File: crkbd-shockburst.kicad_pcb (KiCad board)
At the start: 4 copper layers, 0 parts

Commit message: Layout
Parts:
- added Ant101: antenna, RF_Antenna:Texas_SWRA117D_2.4GHz_Right, F.Cu at (131.8, 53.6)
- added Ant102: antenna, RF_Antenna:Texas_SWRA117D_2.4GHz_Right, F.Cu at (155.8, 53.6)
- added Ant601: antenna, RF_Antenna:Texas_SWRA117D_2.4GHz_Right, F.Cu at (31.6, 128.8)
- added BT201: Battery_Cell, connectors:1x2_2.54mm, F.Cu at (128.8, 72.0)
- added BT501: Battery_Cell, connectors:1x2_2.54mm, F.Cu at (169.2, 69.0)
- added C201: 4.7u, passive:C_0603, F.Cu at (134.1, 69.2)
- added C202: 4.7u, passive:C_0603, F.Cu at (131.3, 71.0)
- added C203: 4.7u, passive:C_0603, F.Cu at (145.7, 59.1)
- added C204: 1u, passive:C_0402, F.Cu at (141.6, 63.5)
- added C205: 100n, passive:C_0402, F.Cu at (139.8, 55.0)
- added C206: 4.7u, passive:C_0603, F.Cu at (145.7, 57.9)
- added C207: 4.7u, passive:C_0603, F.Cu at (145.7, 56.7)
- added C208: 4.7u, passive:C_0603, F.Cu at (144.2, 55.2)
- added C209: 1u, passive:C_0402, F.Cu at (144.1, 63.5)
- added C210: 100n, passive:C_0402, F.Cu at (137.9, 63.5)
- added C211: 100n, passive:C_0402, F.Cu at (145.7, 61.1)
- added C212: 100p, passive:C_0402, F.Cu at (136.4, 60.5)
- added C213: 100n, passive:C_0402, F.Cu at (141.3, 64.8)
- added C214: 820p, passive:C_0402, F.Cu at (136.4, 56.6)
- added C215: 16p, passive:C_0402, F.Cu at (136.4, 63.9)
- added C216: 16p, passive:C_0402, F.Cu at (134.9, 62.2)
- added C219: 100n, passive:C_0402, F.Cu at (139.4, 63.1)
- added C220: ~, passive:C_0402, F.Cu at (131.3, 54.5)
- added C221: ~, passive:C_0402, F.Cu at (131.3, 57.2)
- added C222: 1.2p, passive:C_0402, F.Cu at (134.2, 59.1)
- added C223: 1p, passive:C_0402, F.Cu at (136.8, 59.1)
- added C501: 1u, passive:C_0402, F.Cu at (165.6, 63.5)
- added C502: 100n, passive:C_0402, F.Cu at (165.3, 64.8)
- added C503: 4.7u, passive:C_0603, F.Cu at (168.2, 55.2)
- added C504: 100n, passive:C_0402, F.Cu at (169.7, 61.1)
- added C505: 100p, passive:C_0402, F.Cu at (160.4, 60.5)
- added C506: 820p, passive:C_0402, F.Cu at (160.4, 57.5)
- added C507: 100n, passive:C_0402, F.Cu at (163.8, 55.0)
- added C508: 100n, passive:C_0402, F.Cu at (161.9, 63.5)
- added C509: 1u, passive:C_0402, F.Cu at (168.1, 63.5)
- added C510: 4.7u, passive:C_0603, F.Cu at (169.7, 59.1)
- added C511: 4.7u, passive:C_0603, F.Cu at (169.7, 57.9)
- added C512: 4.7u, passive:C_0603, F.Cu at (169.7, 56.7)
- added C513: ~, passive:C_0402, F.Cu at (155.3, 54.5)
- added C514: ~, passive:C_0402, F.Cu at (155.3, 57.2)
- added C515: 1.2p, passive:C_0402, F.Cu at (158.2, 59.1)
- added C516: 1p, passive:C_0402, F.Cu at (160.8, 59.1)
- added C517: 16p, passive:C_0402, F.Cu at (158.9, 62.2)
- added C518: 16p, passive:C_0402, F.Cu at (160.4, 63.9)
- added C519: 100n, passive:C_0402, F.Cu at (163.4, 63.1)
- added C520: 4.7u, passive:C_0603, F.Cu at (162.8, 68.7)
- added C521: 4.7u, passive:C_0603, F.Cu at (166.4, 67.5)
- added C601: 1u, passive:C_0402, F.Cu at (43.7, 120.7)
- added C602: 100n, passive:C_0402, F.Cu at (43.7, 119.8)
- added C603: 4.7u, passive:C_0603, F.Cu at (35.5, 119.0)
- added C604: 100n, passive:C_0402, F.Cu at (41.4, 117.5)
- added C605: 100p, passive:C_0402, F.Cu at (40.6, 126.8)
- added C606: 820p, passive:C_0402, F.Cu at (37.6, 126.8)
- added C607: 100n, passive:C_0402, F.Cu at (35.2, 123.3)
- added C608: 100n, passive:C_0402, F.Cu at (43.8, 125.1)
- added C609: 1u, passive:C_0402, F.Cu at (43.7, 118.8)
- added C610: 4.7u, passive:C_0603, F.Cu at (39.3, 117.6)
- added C611: 4.7u, passive:C_0603, F.Cu at (38.1, 117.6)
- added C612: 4.7u, passive:C_0603, F.Cu at (36.9, 117.6)
- added C613: ~, passive:C_0402, F.Cu at (32.5, 129.2)
- added C614: ~, passive:C_0402, F.Cu at (35.2, 129.2)
- added C615: 1.2p, passive:C_0402, F.Cu at (37.9, 129.2)
- added C616: 1p, passive:C_0402, F.Cu at (39.3, 126.3)
- added C617: 16p, passive:C_0402, F.Cu at (44.2, 127.2)
- added C618: 16p, passive:C_0402, F.Cu at (44.2, 126.2)
- added D201: RED, Diode_SMD:D_0603_1608Metric, F.Cu at (146.2, 54.6)
- added D301: BAT43W, Diode_SMD:D_SOD-123, F.Cu at (31.2, 65.2)
- added D302: BAT43W, Diode_SMD:D_SOD-123, F.Cu at (50.2, 65.2)
- added D303: BAT43W, Diode_SMD:D_SOD-123, F.Cu at (69.2, 60.2)
- added D304: BAT43W, Diode_SMD:D_SOD-123, F.Cu at (88.2, 57.8)
- added D305: BAT43W, Diode_SMD:D_SOD-123, F.Cu at (107.2, 60.2)
- added D306: BAT43W, Diode_SMD:D_SOD-123, F.Cu at (126.2, 62.8)
- added D307: BAT43W, Diode_SMD:D_SOD-123, F.Cu at (31.2, 84.2)
- added D308: BAT43W, Diode_SMD:D_SOD-123, F.Cu at (50.2, 84.2)
- added D309: BAT43W, Diode_SMD:D_SOD-123, F.Cu at (69.2, 79.2)
- added D310: BAT43W, Diode_SMD:D_SOD-123, F.Cu at (88.2, 76.8)
- added D311: BAT43W, Diode_SMD:D_SOD-123, F.Cu at (107.2, 79.2)
- added D312: BAT43W, Diode_SMD:D_SOD-123, F.Cu at (126.2, 81.9)
- added D313: BAT43W, Diode_SMD:D_SOD-123, F.Cu at (31.2, 103.2)
- added D314: BAT43W, Diode_SMD:D_SOD-123, F.Cu at (50.2, 103.2)
- added D315: BAT43W, Diode_SMD:D_SOD-123, F.Cu at (69.2, 98.2)
- added D316: BAT43W, Diode_SMD:D_SOD-123, F.Cu at (88.2, 95.8)
- added D317: BAT43W, Diode_SMD:D_SOD-123, F.Cu at (107.2, 98.2)
- added D318: BAT43W, Diode_SMD:D_SOD-123, F.Cu at (126.2, 100.8)
- added D319: BAT43W, Diode_SMD:D_SOD-123, F.Cu at (97.2, 112.8)
- added D320: BAT43W, Diode_SMD:D_SOD-123, F.Cu at (117.0, 112.0)
- added D321: BAT43W, Diode_SMD:D_SOD-123, F.Cu at (127.8, 112.8)
- added D401: BAT43W, Diode_SMD:D_SOD-123, F.Cu at (266.8, 65.2)
- added D402: BAT43W, Diode_SMD:D_SOD-123, F.Cu at (247.8, 65.2)
- added D403: BAT43W, Diode_SMD:D_SOD-123, F.Cu at (228.8, 60.2)
- added D404: BAT43W, Diode_SMD:D_SOD-123, F.Cu at (209.8, 57.8)
- added D405: BAT43W, Diode_SMD:D_SOD-123, F.Cu at (190.8, 60.2)
- added D406: BAT43W, Diode_SMD:D_SOD-123, F.Cu at (171.8, 62.8)
- added D407: BAT43W, Diode_SMD:D_SOD-123, F.Cu at (266.8, 84.2)
- added D408: BAT43W, Diode_SMD:D_SOD-123, F.Cu at (247.8, 84.2)
- added D409: BAT43W, Diode_SMD:D_SOD-123, F.Cu at (228.8, 79.2)
- added D410: BAT43W, Diode_SMD:D_SOD-123, F.Cu at (209.8, 76.8)
- added D411: BAT43W, Diode_SMD:D_SOD-123, F.Cu at (190.8, 79.2)
- added D412: BAT43W, Diode_SMD:D_SOD-123, F.Cu at (171.8, 81.9)
- added D413: BAT43W, Diode_SMD:D_SOD-123, F.Cu at (266.8, 103.2)
- added D414: BAT43W, Diode_SMD:D_SOD-123, F.Cu at (247.8, 103.2)
- added D415: BAT43W, Diode_SMD:D_SOD-123, F.Cu at (228.8, 98.2)
- added D416: BAT43W, Diode_SMD:D_SOD-123, F.Cu at (209.8, 95.8)
- added D417: BAT43W, Diode_SMD:D_SOD-123, F.Cu at (190.8, 98.2)
- added D418: BAT43W, Diode_SMD:D_SOD-123, F.Cu at (171.8, 100.8)
- added D419: BAT43W, Diode_SMD:D_SOD-123, F.Cu at (200.8, 112.8)
- added D420: BAT43W, Diode_SMD:D_SOD-123, F.Cu at (181.0, 112.0)
- added D421: BAT43W, Diode_SMD:D_SOD-123, F.Cu at (170.2, 112.8)
- added D501: RED, Diode_SMD:D_0603_1608Metric, F.Cu at (151.8, 54.6)
- added D601: RED, Diode_SMD:D_0603_1608Metric, F.Cu at (34.7, 117.1)
- added FB201: FerriteBead_Small, passive:R_0603, F.Cu at (134.1, 71.6)
- added FB501: FerriteBead_Small, passive:R_0603, F.Cu at (161.5, 68.7)
- added FB601: FerriteBead_Small, passive:R_0603, F.Cu at (45.9, 120.5)
- added H201: MountingHole, MountingHole:MountingHole_4.3mm_M4, F.Cu at (31.8, 93.8)
- added H202: MountingHole, MountingHole:MountingHole_4.3mm_M4, F.Cu at (31.8, 74.8)
- added H203: MountingHole, MountingHole:MountingHole_4.3mm_M4, F.Cu at (74.9, 111.0)
- added H204: MountingHole, MountingHole:MountingHole_4.3mm_M4, F.Cu at (107.7, 71.2)
- added H205: MountingHole, MountingHole:MountingHole_4.3mm_M4, F.Cu at (121.5, 118.6)
- added H501: MountingHole, MountingHole:MountingHole_4.3mm_M4, F.Cu at (266.2, 93.8)
- added H502: MountingHole, MountingHole:MountingHole_4.3mm_M4, F.Cu at (266.2, 74.8)
- added H503: MountingHole, MountingHole:MountingHole_4.3mm_M4, F.Cu at (223.1, 111.0)
- added H504: MountingHole, MountingHole:MountingHole_4.3mm_M4, F.Cu at (190.3, 71.2)
- added H505: MountingHole, MountingHole:MountingHole_4.3mm_M4, F.Cu at (176.5, 118.6)
- added J201: USB_C_Receptacle_USB2.0, connectors:USB_C_Receptacle_USB4105, F.Cu at (144.2, 71.8)
- added J202: tag-connect-swd, Connector:Tag-Connect_TC2030-IDC-NL_2x03_P1.27mm_Vertical, F.Cu at (131.2, 63.2)
- added J5: Breakaway_Tabs, kbd:Breakaway_Tabs, F.Cu at (31.7, 55.8)
- added J5: Breakaway_Tabs, kbd:Breakaway_Tabs, F.Cu at (266.3, 55.8)
- added J5: Breakaway_Tabs, kbd:Breakaway_Tabs, F.Cu at (199.2, 130.0)
- added J5: Breakaway_Tabs, kbd:Breakaway_Tabs, F.Cu at (45.8, 132.2)
- added J5: Breakaway_Tabs, kbd:Breakaway_Tabs, F.Cu at (45.8, 116.2)
- added J5: Breakaway_Tabs, kbd:Breakaway_Tabs, F.Cu at (252.3, 112.7)
- added J5: Breakaway_Tabs, kbd:Breakaway_Tabs, F.Cu at (160.2, 47.8)
- added J5: Breakaway_Tabs, kbd:Breakaway_Tabs, F.Cu at (136.2, 47.8)
- added J5: Breakaway_Tabs, kbd:Breakaway_Tabs, F.Cu at (45.8, 112.7)
- added J5: Breakaway_Tabs, kbd:Breakaway_Tabs, F.Cu at (25.8, 124.3)
- added J5: Breakaway_Tabs, kbd:Breakaway_Tabs, F.Cu at (99.1, 130.1)
- added J501: tag-connect-swd, Connector:Tag-Connect_TC2030-IDC-NL_2x03_P1.27mm_Vertical, F.Cu at (155.2, 62.8)
- added J502: USB_C_Receptacle_USB2.0, connectors:USB_C_Receptacle_USB4105, F.Cu at (153.8, 71.8)
- added J601: tag-connect-swd, Connector:Tag-Connect_TC2030-IDC-NL_2x03_P1.27mm_Vertical, B.Cu at (34.7, 124.0)
- added J602: USB_A, usb:USB_A_1001-011-01101, F.Cu at (49.5, 124.2)
- added L201: 10u, passive:R_0603, F.Cu at (143.0, 63.9)
- added L202: 47n, passive:R_0402, F.Cu at (142.7, 65.5)
- added L203: ~, passive:R_0402, F.Cu at (131.8, 55.9)
- added L204: 4.7n, passive:R_0402, F.Cu at (135.5, 58.6)
- added L205: 2.2n, passive:R_0402, F.Cu at (132.8, 58.6)
- added L501: 47n, passive:R_0402, F.Cu at (166.7, 65.5)
- added L502: 10u, passive:R_0603, F.Cu at (167.0, 63.9)
- added L503: ~, passive:R_0402, F.Cu at (155.8, 55.9)
- added L504: 2.2n, passive:R_0402, F.Cu at (156.8, 58.6)
- added L505: 4.7n, passive:R_0402, F.Cu at (159.5, 58.6)
- added L603: ~, passive:R_0402, F.Cu at (33.8, 128.8)
- added L604: 2.2n, passive:R_0402, F.Cu at (36.5, 128.8)
- added L605: 4.7n, passive:R_0402, F.Cu at (38.9, 127.7)
- added R101: 1k, passive:R_0402, F.Cu at (136.4, 57.6)
- added R201: 1M, passive:R_0402, F.Cu at (139.4, 65.0)
- added R202: 1M, passive:R_0402, F.Cu at (139.4, 64.0)
- added R203: 5.1k, passive:R_0402, F.Cu at (145.1, 65.3)
- added R204: 5.1k, passive:R_0402, F.Cu at (144.1, 65.3)
- added R205: 1k, passive:R_0402, F.Cu at (145.7, 60.2)
- added R206: 5.1k, passive:R_0402, F.Cu at (134.3, 67.5)
- added R501: 1k, passive:R_0402, F.Cu at (169.7, 60.2)
- added R502: 1M, passive:R_0402, F.Cu at (163.4, 65.0)
- added R503: 1M, passive:R_0402, F.Cu at (163.4, 64.0)
- added R504: 5.1k, passive:R_0402, F.Cu at (158.2, 64.9)
- added R505: 5.1k, passive:R_0402, F.Cu at (158.2, 65.9)
- added R506: 5.1k, passive:R_0402, F.Cu at (164.3, 72.1)
- added R601: 1k, passive:R_0402, F.Cu at (40.4, 117.5)
- added SW301: SW_Push, connectors:Kailh MX hotswap socket, B.Cu at (22.2, 65.2)
- added SW302: SW_Push, connectors:Kailh MX hotswap socket, B.Cu at (41.2, 65.2)
- added SW303: SW_Push, connectors:Kailh MX hotswap socket, B.Cu at (60.2, 60.2)
- added SW304: SW_Push, connectors:Kailh MX hotswap socket, B.Cu at (79.2, 57.8)
- added SW305: SW_Push, connectors:Kailh MX hotswap socket, B.Cu at (98.2, 60.2)
- added SW306: SW_Push, connectors:Kailh MX hotswap socket, B.Cu at (117.2, 62.8)
- added SW307: SW_Push, connectors:Kailh MX hotswap socket, B.Cu at (22.2, 84.2)
- added SW308: SW_Push, connectors:Kailh MX hotswap socket, B.Cu at (41.2, 84.2)
- added SW309: SW_Push, connectors:Kailh MX hotswap socket, B.Cu at (60.2, 79.2)
- added SW310: SW_Push, connectors:Kailh MX hotswap socket, B.Cu at (79.2, 76.8)
- added SW311: SW_Push, connectors:Kailh MX hotswap socket, B.Cu at (98.2, 79.2)
- added SW312: SW_Push, connectors:Kailh MX hotswap socket, B.Cu at (117.2, 81.8)
- added SW313: SW_Push, connectors:Kailh MX hotswap socket, B.Cu at (22.2, 103.2)
- added SW314: SW_Push, connectors:Kailh MX hotswap socket, B.Cu at (41.2, 103.2)
- added SW315: SW_Push, connectors:Kailh MX hotswap socket, B.Cu at (60.2, 98.2)
- added SW316: SW_Push, connectors:Kailh MX hotswap socket, B.Cu at (79.2, 95.8)
- added SW317: SW_Push, connectors:Kailh MX hotswap socket, B.Cu at (98.2, 98.2)
- added SW318: SW_Push, connectors:Kailh MX hotswap socket, B.Cu at (117.2, 100.8)
- added SW319: SW_Push, connectors:Kailh MX hotswap socket, B.Cu at (88.2, 118.2)
- added SW320: SW_Push, connectors:Kailh MX hotswap socket, B.Cu at (109.8, 120.8)
- added SW321: SW_Push, connectors:Kailh MX hotswap socket 1.5u, B.Cu at (132.1, 124.5)
- added SW401: SW_Push, connectors:Kailh MX hotswap socket, B.Cu at (275.8, 65.2)
- added SW402: SW_Push, connectors:Kailh MX hotswap socket, B.Cu at (256.8, 65.2)
- added SW403: SW_Push, connectors:Kailh MX hotswap socket, B.Cu at (237.8, 60.2)
- added SW404: SW_Push, connectors:Kailh MX hotswap socket, B.Cu at (218.8, 57.8)
- added SW405: SW_Push, connectors:Kailh MX hotswap socket, B.Cu at (199.8, 60.2)
- added SW406: SW_Push, connectors:Kailh MX hotswap socket, B.Cu at (180.8, 62.8)
- added SW407: SW_Push, connectors:Kailh MX hotswap socket, B.Cu at (275.8, 84.2)
- added SW408: SW_Push, connectors:Kailh MX hotswap socket, B.Cu at (256.8, 84.2)
- added SW409: SW_Push, connectors:Kailh MX hotswap socket, B.Cu at (237.8, 79.2)
- added SW410: SW_Push, connectors:Kailh MX hotswap socket, B.Cu at (218.8, 76.8)
- added SW411: SW_Push, connectors:Kailh MX hotswap socket, B.Cu at (199.8, 79.2)
- added SW412: SW_Push, connectors:Kailh MX hotswap socket, B.Cu at (180.8, 81.8)
- added SW413: SW_Push, connectors:Kailh MX hotswap socket, B.Cu at (275.8, 103.2)
- added SW414: SW_Push, connectors:Kailh MX hotswap socket, B.Cu at (256.8, 103.2)
- added SW415: SW_Push, connectors:Kailh MX hotswap socket, B.Cu at (237.8, 98.2)
- added SW416: SW_Push, connectors:Kailh MX hotswap socket, B.Cu at (218.8, 95.8)
- added SW417: SW_Push, connectors:Kailh MX hotswap socket, B.Cu at (199.8, 98.2)
- added SW418: SW_Push, connectors:Kailh MX hotswap socket, B.Cu at (180.8, 100.8)
- added SW419: SW_Push, connectors:Kailh MX hotswap socket, B.Cu at (209.8, 118.2)
- added SW420: SW_Push, connectors:Kailh MX hotswap socket, B.Cu at (188.2, 120.8)
- added SW421: SW_Push, connectors:Kailh MX hotswap socket 1.5u, B.Cu at (165.9, 124.5)
- added SW601: SW_Push, Button_Switch_SMD:SW_SPST_EVQP2, F.Cu at (43.5, 129.9)
- added U201: nRF52833-QDxx, Package_DFN_QFN:QFN-40-1EP_5x5mm_P0.4mm_EP3.6x3.6mm, F.Cu at (141.0, 59.2)
- added U202: USBLC6-2SC6, Package_TO_SOT_SMD:SOT-23-6, F.Cu at (136.8, 71.8)
- added U204: MCP73832-2-OT, Package_TO_SOT_SMD:SOT-23-5, F.Cu at (131.3, 68.6)
- added U501: nRF52833-QDxx, Package_DFN_QFN:QFN-40-1EP_5x5mm_P0.4mm_EP3.6x3.6mm, F.Cu at (165.0, 59.2)
- added U502: USBLC6-2SC6, Package_TO_SOT_SMD:SOT-23-6, F.Cu at (161.2, 71.8)
- added U503: MCP73832-2-OT, Package_TO_SOT_SMD:SOT-23-5, F.Cu at (165.5, 69.8)
- added U601: nRF52833-QDxx, Package_DFN_QFN:QFN-40-1EP_5x5mm_P0.4mm_EP3.6x3.6mm, F.Cu at (39.5, 122.2)
- added U602: USBLC6-2SC6, Package_TO_SOT_SMD:SOT-23-6, F.Cu at (45.1, 123.0)
- added Y201: 32 MHz, crystals:Crystal_4Pin_2.0x1.6mm, F.Cu at (136.4, 62.1)
- added Y501: 32 MHz, crystals:Crystal_4Pin_2.0x1.6mm, F.Cu at (160.4, 62.1)
- added Y601: 32 MHz, crystals:Crystal_4Pin_2.0x1.6mm, F.Cu at (42.4, 126.7)
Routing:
- net /Right Keyboard Controller/KIO0: track 0.00 -> 256.9 mm, vias 0 -> 1
- net /Left Keyboard Controller/KIO4: track 0.00 -> 253.3 mm, vias 0 -> 1
- net /Right Keyboard Controller/KIO1: track 0.00 -> 240.0 mm, vias 0 -> 1
- net /Left Keyboard Controller/KIO5: track 0.00 -> 232.5 mm, vias 0 -> 1
- net /Right Keyboard Controller/KIO2: track 0.00 -> 220.2 mm, vias 0 -> 1
- net /Left Keyboard Controller/KIO6: track 0.00 -> 212.6 mm, vias 0 -> 1
- net /Left Keyboard Controller/KIO7: track 0.00 -> 201.3 mm, vias 0 -> 1
- net /Right Keyboard Controller/KIO3: track 0.00 -> 201.0 mm, vias 0 -> 1
- net /Right Keyboard Controller/KIO9: track 0.00 -> 178.8 mm, vias 0 -> 1
- net /Left Keyboard Controller/KIO8: track 0.00 -> 178.0 mm, vias 0 -> 1
- net /Left Keyboard Controller/KIO2: track 0.00 -> 157.8 mm, vias 0 -> 2
- net /Left Keyboard Controller/KIO9: track 0.00 -> 157.7 mm, vias 0 -> 1
- net /Right Keyboard Controller/KIO8: track 0.00 -> 157.4 mm, vias 0 -> 1
- net /Right Keyboard Controller/KIO6: track 0.00 -> 149.6 mm, vias 0 -> 2
- net /Left Keyboard Controller/KIO1: track 0.00 -> 140.5 mm, vias 0 -> 2
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- added copper zone on B.Cu, net GND
- added copper zone on F.Cu, net GND
- added copper zone on In1.Cu, net GND
- added copper zone on In2.Cu, net GND
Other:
- board outline added: 272 x 112 mm
- board text added: "+"
- board text added: "-"
- board text added: "502030 Li-Ion"
- board text added: "BAT"
- board text added: "BATTERY"
- board text added: "By Emil Fresk - @korken89"
- board text added: "Chg = 200 mA"
- board text added: "Corne ShockBurst"
- board text added: "Dongle"
- board text added: "Emil Fresk @korken89"
- board text added: "Rev 1.0"
- board text added: "TM"

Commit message: Save
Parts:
- added REF**: Hirose_FH12-10S-0.5SH_1x10-1MP_P0.50mm_Horizontal, Connector_FFC-FPC:Hirose_FH12-10S-0.5SH_1x10-1MP_P0.50mm_Horizontal, B.Cu at (137.0, 60.0)
- SW301, SW302, SW303, SW304, SW305, SW306, SW307, SW308, SW309, SW310, SW311, SW312, SW313, SW314, SW315, SW316, SW317, SW318, SW319, SW320, SW321, SW401, SW402, SW403, SW404, SW405, SW406, SW407, SW408, SW409, SW410, SW411, SW412, SW413, SW414, SW415, SW416, SW417, SW418, SW419, SW420, SW421: moved to F.Cu
- moved D419 18.5 mm to (217.5, 120.5)
- moved D319 17.6 mm to (80.5, 118.0)
- moved D421 17.6 mm to (175.5, 129.5)
- moved D420 17.5 mm to (196.0, 121.0)
- moved D320 16.8 mm to (102.0, 119.5)
- moved D301 16.8 mm to (14.5, 65.2)
- moved D302 16.8 mm to (33.5, 65.2)
- moved D303 16.8 mm to (52.5, 60.2)
- moved D304 16.8 mm to (71.5, 57.8)
- moved D305 16.8 mm to (90.5, 60.2)
- moved D306 16.8 mm to (109.5, 62.8)
- moved D307 16.8 mm to (14.5, 84.2)
- moved D308 16.8 mm to (33.5, 84.2)
- moved D309 16.8 mm to (52.5, 79.2)
- moved D310 16.8 mm to (71.5, 76.8)
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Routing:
- net /Right Keyboard Controller/KIO0: track 256.9 -> 84.1 mm
- net /Right Keyboard Controller/KIO1: track 240.0 -> 86.3 mm
- net /Right Keyboard Controller/KIO2: track 220.2 -> 84.4 mm
- net /Right Keyboard Controller/KIO3: track 201.0 -> 75.8 mm
- net /Right Keyboard Controller/KIO6: track 149.6 -> 43.7 mm
- net /Right Keyboard Controller/KIO5: track 132.3 -> 27.5 mm
- net /Right Keyboard Controller/KIO4: track 112.0 -> 7.41 mm
- net /Right Keyboard Controller/KIO9: track 178.8 -> 74.3 mm
- net /Right Keyboard Controller/KIO8: track 157.4 -> 73.0 mm
- net /Left Keyboard Controller/KIO9: track 157.7 -> 105.4 mm, vias 1 -> 5
- net /Right Keyboard Controller/KIO7: track 90.3 -> 44.9 mm
- net /Left Keyboard Controller/KIO3: track 90.3 -> 119.7 mm
- net /Left Keyboard Controller/KIO1: track 140.5 -> 159.2 mm
- net /Left Keyboard Controller/KIO0: track 120.0 -> 138.2 mm
- net /Left Keyboard Controller/KIO2: track 157.8 -> 175.7 mm
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
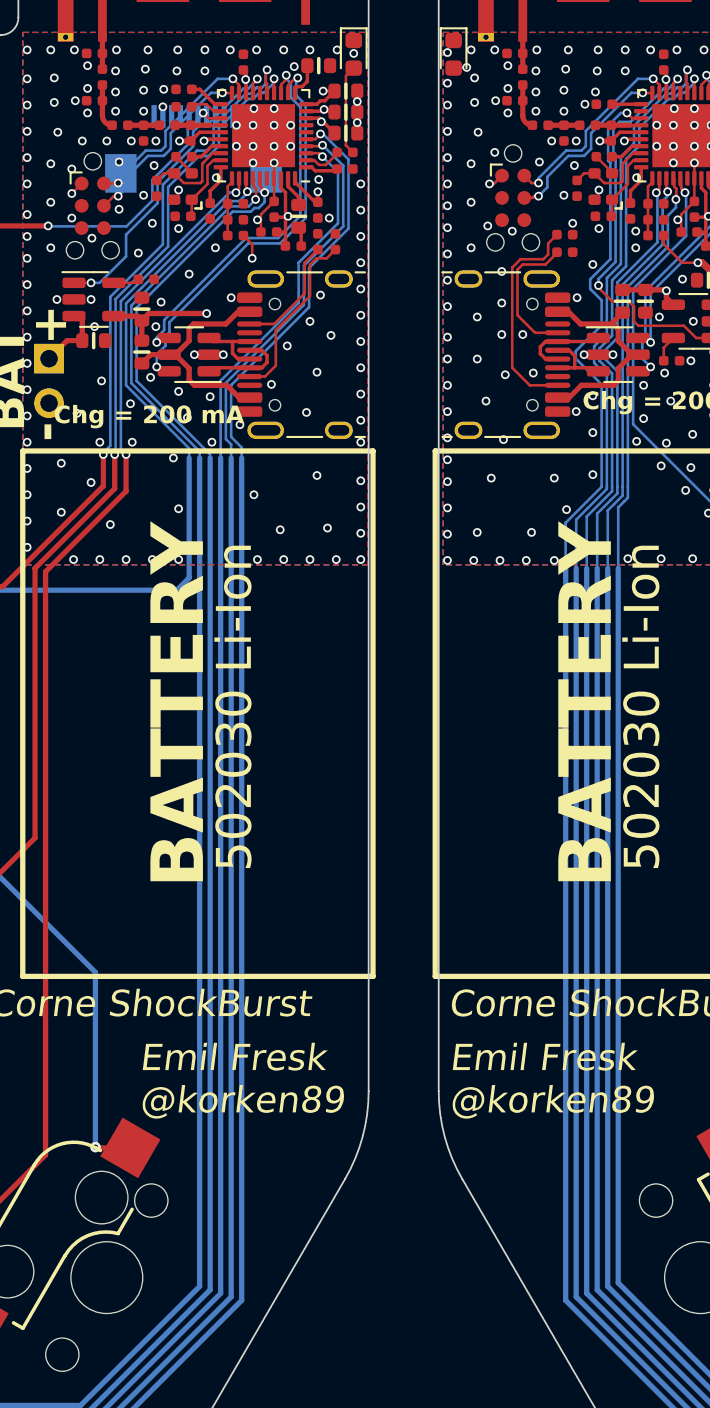
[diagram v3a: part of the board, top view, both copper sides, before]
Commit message: Testing memory pixel display
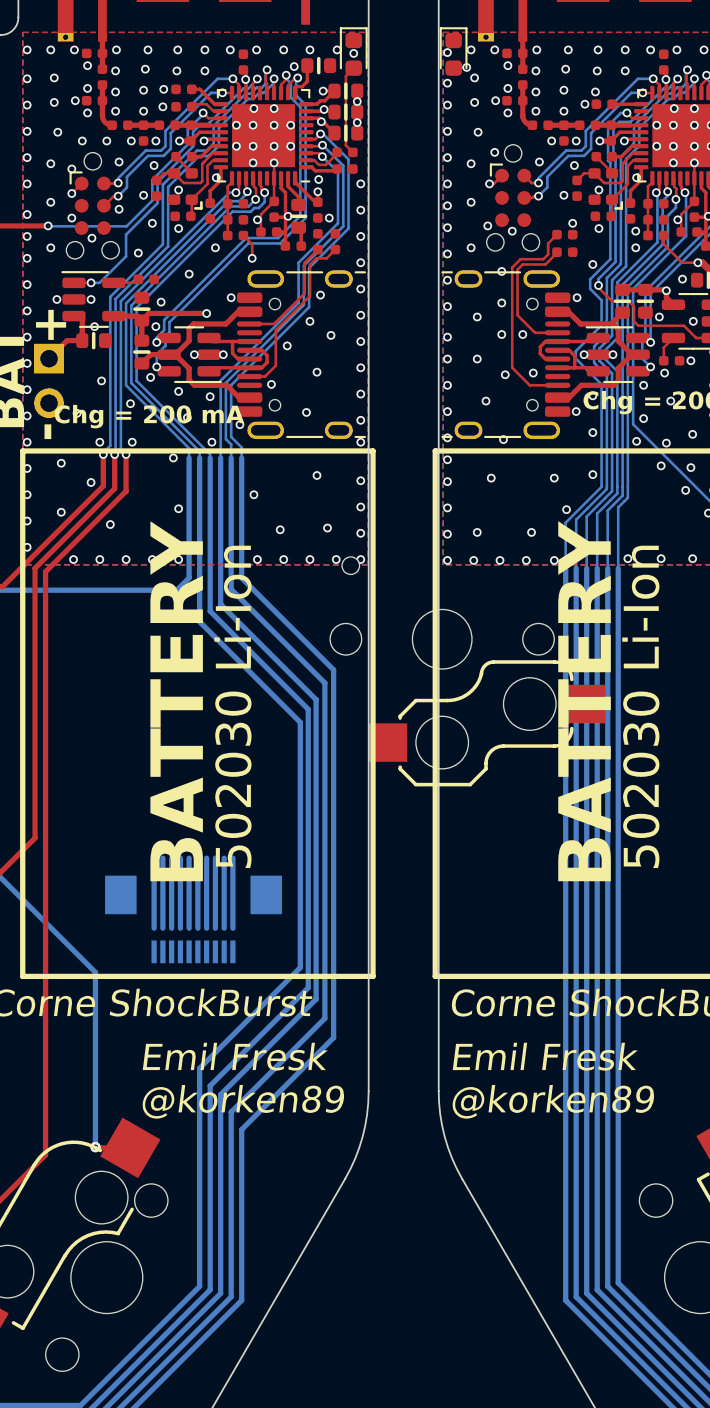
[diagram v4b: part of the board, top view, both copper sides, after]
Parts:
- added REF**: Kailh Choc Hotswap 1U, connectors:Kailh Choc Hotswap 1U, F.Cu at (151.2, 88.0)
- moved REF** 44.0 mm to (137.0, 104.0), turned to 0 degrees
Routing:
- net /Left Keyboard Controller/KIO8: track 171.2 -> 176.0 mm
- net /Left Keyboard Controller/KIO7: track 192.0 -> 196.6 mm
- net /Left Keyboard Controller/KIO6: track 207.4 -> 211.9 mm
- net /Left Keyboard Controller/KIO5: track 220.3 -> 224.7 mm
- net /Left Keyboard Controller/KIO4: track 241.7 -> 246.0 mm
